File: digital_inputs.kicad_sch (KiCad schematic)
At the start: 11 parts, among them J2 Samtec Isorate Right Angle, J3 Samtec Isorate, U8 SN74LVC16244A-EP

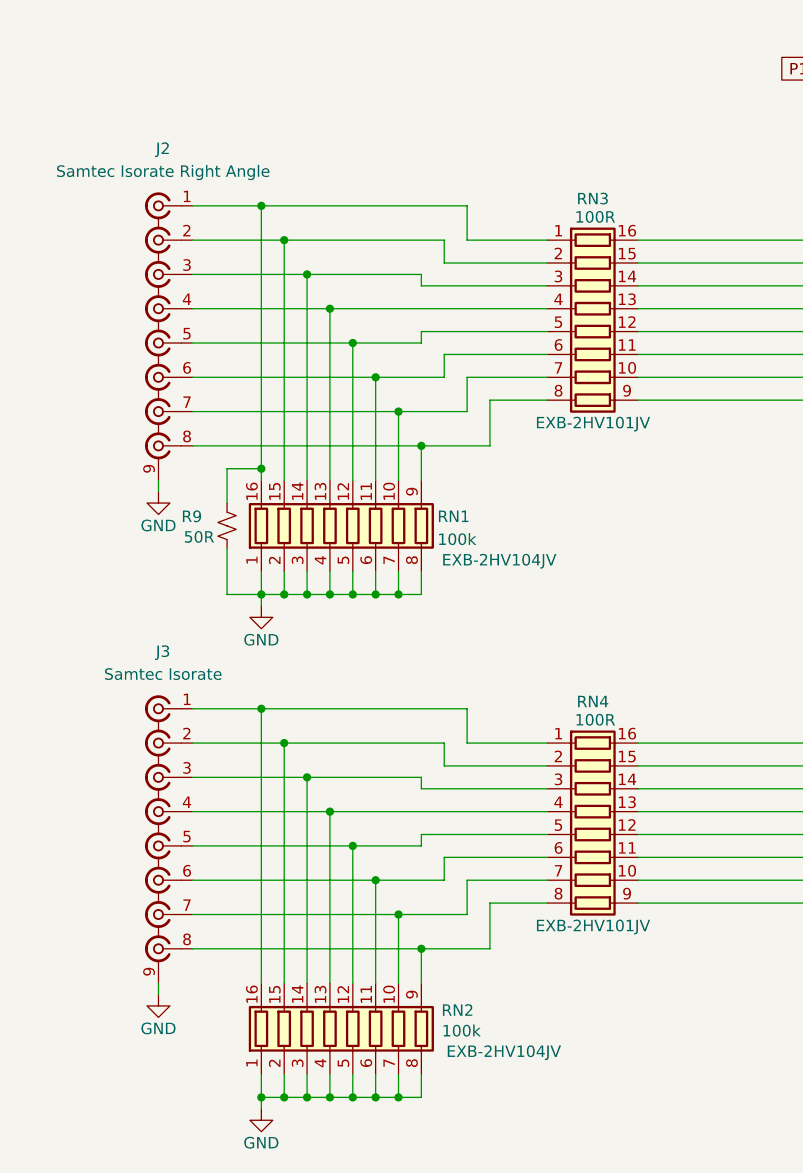
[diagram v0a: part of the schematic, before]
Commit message: Schematic updates
- Changed Connecters to MMCX
- Added Test points on clocks and data buses
- Added attenuation before the RF input level detection IC to better keep the recommended input within its linear range
- Added a low pass filter at the input of the RF input level detection IC
- grounded the thermal pad of the ADC
- added some additional decoupling caps in for the clock splitter chip (to be in line with what is on Zest)
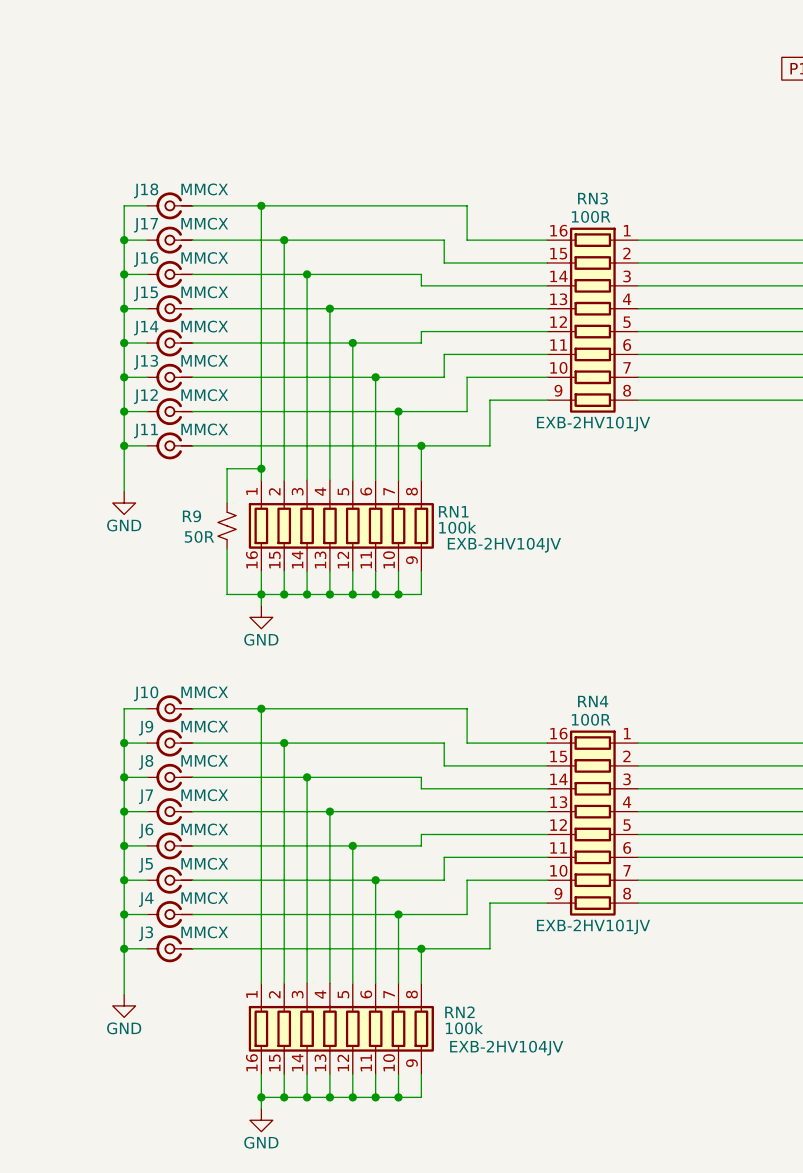
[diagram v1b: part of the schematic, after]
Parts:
- removed J2: Samtec Isorate Right Angle, rf-input-fmc:SAMTEC_IP5-08-01-L-S-RA1-L-TR, symbol rf-input-fmc:Isorate_8pin
- removed J3: Samtec Isorate, rf-input-fmc:SAMTEC_IP5-08-05.0-L-S-1-L-TR, symbol rf-input-fmc:Isorate_8pin
- added J10, J11, J12, J13, J14, J15, J16, J17, J18, J3, J4, J5, J6, J7, J8, J9: MMCX, Connector_Coaxial:MMCX_Molex_73415-1471_Vertical, symbol Connector:Conn_Coaxial_Small
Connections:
- net GND: now also RN1.10 (R7.2), RN1.11 (R6.2), RN1.12 (R5.2), RN1.13 (R4.2), RN1.14 (R3.2), RN1.15 (R2.2), RN1.16 (R1.2), RN1.9 (R8.2), RN2.10 (R7.2), RN2.11 (R6.2), RN2.12 (R5.2), RN2.13 (R4.2), RN2.14 (R3.2), RN2.15 (R2.2), RN2.16 (R1.2), RN2.9 (R8.2), J10.2 (Ext), J11.2 (Ext), J12.2 (Ext), J13.2 (Ext), J14.2 (Ext), J15.2 (Ext), J16.2 (Ext), J17.2 (Ext), J18.2 (Ext), J3.2 (Ext), J4.2 (Ext), J5.2 (Ext), J6.2 (Ext), J7.2 (Ext), J8.2 (Ext), J9.2 (Ext); no longer RN1.1 (R1.1), RN1.2 (R2.1), RN1.3 (R3.1), RN1.4 (R4.1), RN1.5 (R5.1), RN1.6 (R6.1), RN1.7 (R7.1), RN1.8 (R8.1), RN2.1 (R1.1), RN2.2 (R2.1), RN2.3 (R3.1), RN2.4 (R4.1), RN2.5 (R5.1), RN2.6 (R6.1), RN2.7 (R7.1), RN2.8 (R8.1)
- net at RN4.7 (R7.1): now also U8.27 (4A3); no longer RN2.10 (R7.2)
- net at RN4.6 (R6.1): now also U8.29 (4A2); no longer RN2.11 (R6.2)
- net at RN4.5 (R5.1): now also U8.30 (4A1); no longer RN2.12 (R5.2)
- net at RN4.4 (R4.1): now also U8.32 (3A4); no longer RN2.13 (R4.2)
- net at RN4.3 (R3.1): now also U8.33 (3A3); no longer RN2.14 (R3.2)
- net at RN4.2 (R2.1): now also U8.35 (3A2); no longer RN2.15 (R2.2)
- net at RN4.1 (R1.1): now also U8.36 (3A1); no longer RN2.16 (R1.2)
- net at RN4.8 (R8.1): now also U8.26 (4A4); no longer RN2.9 (R8.2)
- net at RN3.2 (R2.1): now also U8.46 (1A2); no longer RN1.15 (R2.2)
- net at RN3.3 (R3.1): now also U8.44 (1A3); no longer RN1.14 (R3.2)
- net at RN3.4 (R4.1): now also U8.43 (1A4); no longer RN1.13 (R4.2)
- net at RN3.5 (R5.1): now also U8.41 (2A1); no longer RN1.12 (R5.2)
- net at RN3.6 (R6.1): now also U8.40 (2A2); no longer RN1.11 (R6.2)
- net at RN3.7 (R7.1): now also U8.38 (2A3); no longer RN1.10 (R7.2)
- net at RN3.8 (R8.1): now also U8.37 (2A4); no longer RN1.9 (R8.2)
- net at RN4.9 (R8.2): now also RN2.8 (R8.1), J3.1 (In); no longer U8.26 (4A4)
- net at RN4.10 (R7.2): now also RN2.7 (R7.1), J4.1 (In); no longer U8.27 (4A3)
- net at RN4.11 (R6.2): now also RN2.6 (R6.1), J5.1 (In); no longer U8.29 (4A2)
- net at RN4.12 (R5.2): now also RN2.5 (R5.1), J6.1 (In); no longer U8.30 (4A1)
- net at RN4.13 (R4.2): now also RN2.4 (R4.1), J7.1 (In); no longer U8.32 (3A4)
- net at RN4.14 (R3.2): now also RN2.3 (R3.1), J8.1 (In); no longer U8.33 (3A3)
- net at RN4.15 (R2.2): now also RN2.2 (R2.1), J9.1 (In); no longer U8.35 (3A2)
- net at RN4.16 (R1.2): now also RN2.1 (R1.1), J10.1 (In); no longer U8.36 (3A1)
- net at RN3.9 (R8.2): now also RN1.8 (R8.1), J11.1 (In); no longer U8.37 (2A4)
- net at RN3.10 (R7.2): now also RN1.7 (R7.1), J12.1 (In); no longer U8.38 (2A3)
- net at RN3.11 (R6.2): now also RN1.6 (R6.1), J13.1 (In); no longer U8.40 (2A2)
- net at RN3.12 (R5.2): now also RN1.5 (R5.1), J14.1 (In); no longer U8.41 (2A1)
- net at RN3.13 (R4.2): now also RN1.4 (R4.1), J15.1 (In); no longer U8.43 (1A4)
- net at RN3.14 (R3.2): now also RN1.3 (R3.1), J16.1 (In); no longer U8.44 (1A3)
- net at RN3.15 (R2.2): now also RN1.2 (R2.1), J17.1 (In); no longer U8.46 (1A2)
- net at RN3.16 (R1.2): now also R9.1, RN1.1 (R1.1), J18.1 (In); no longer U8.47 (1A1)
- new net: RN3.1 (R1.1), U8.47 (1A1)
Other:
- moved on the sheet: RN3, RN4

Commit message: Updated BOM of all parts
Updated BOM of all parts
-added supplier & supplier part number to all parts
- fixed many issues with part including:R5-R8,C34,C35,C24, R10-R15

Changed filter C36&C37 to 15nF (keep COG & 0603, but changes filter cutoff to 3.8kHz|was 12kHz)
Changed bulk Caps to 22uF (was 47uF) to get a Cap with enough voltage headroom at 12V while 0805
Changed C31 to be a bulk 10uF cap
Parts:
- removed L7: 0603, Inductor_SMD:L_0603_1608Metric, symbol Device:L_Ferrite_Small
- C31: value 100nF -> 10uF; footprint Capacitor_SMD:C_0402_1005Metric -> Capacitor_SMD:C_0603_1608Metric; MPN GRM155R61A104KA01D -> GRM188R6YA106MA73D; Manufacturer Murata -> Murata Electronics; Supplier (none) -> Digikey; Supplier Part Number (none) -> 490-13248-1-ND
- C32: MPN GRM155R61A104KA01D -> GCM155R71H104KE02J; Manufacturer Murata -> Murata Electronics; Supplier (none) -> Digikey; Supplier Part Number (none) -> 490-14514-1-ND
- J10, J11, J12, J13, J14, J15, J16, J17, J18, J3, J4, J5, J6, J7, J8, J9: Supplier (none) -> Digikey; Supplier Part Number (none) -> SAM10617-ND
- R9: Supplier (none) -> Digikey; Supplier Part Number (none) -> 541-TNPW120650R0BEENCT-ND
- RN1, RN2: Supplier (none) -> Digikey; Supplier Part Number (none) -> Y1104CT-ND
- RN3, RN4: Supplier (none) -> Digikey; Supplier Part Number (none) -> Y1101CT-ND
- U8: Supplier (none) -> Digikey; Supplier Part Number (none) -> 296-36050-5-ND
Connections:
- net GND: now also C31.2; no longer C31.1
- net P1_VADJ: now also C31.1, C32.2, U8.18 (VCC), U8.31 (VCC), U8.42 (VCC), U8.7 (VCC)

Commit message: Finished Board Layout
Schematic Changes
- Removed some testpoints
- Fixed Lib issues
- moved around FMC pinout

Layout
- routed all traces
- routed RF traces using Controlled Impedance in mind
- ERC/DRC free
- All silkscreen is arranged

Still to do
- finish net-classes for controlled traces
- create arc traces for diff CLK lines
- small tweaks to improve RF performance
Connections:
- net D_Input11: now also U8.17 (3Y4); no longer U8.23 (4Y4)
- net D_Input12: now also U8.19 (4Y1); no longer U8.13 (3Y1)
- net D_Input15: now also U8.23 (4Y4); no longer U8.17 (3Y4)
- net D_Input8: now also U8.13 (3Y1); no longer U8.19 (4Y1)

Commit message: Tweaks to Layout/ fixed project errors
-Adjusted Testpoints by changing the value field to visible on the silkscreen layer.
- Fixed DRC and ERC issues

Known to do:
- run rounded traces
- determine neg/gnd pin of J20 (do we want to float but diff? SE?)
- determine/implement best practice grounding for mounting holes?
- Additional RF trace tweaking
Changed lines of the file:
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@@
 	)
 	(junction
-		(at 149.86 41.91)
-		(diameter 0)
-		(color 0 0 0 0)
-	)
-	(junction
 		(at 71.12 100.33)
 		(diameter 0)
@@
 					(unit 1)
 				)
-			)
-		)
-	)
-	(symbol
-		(lib_id "power:PWR_FLAG")
-		(at 149.86 41.91 270)
-		(mirror x)
-		(unit 1)
-		(exclude_from_sim no)
-		(in_bom yes)
-		(on_board yes)
-		(dnp no)
-		(fields_autoplaced yes)
-		(property "Reference" "#FLG04"
-			(at 151.765 41.91 0)
-			(effects
-				(font
-					(size 1.27 1.27)
-				)
-				(hide yes)
-			)
-		)
-		(property "Value" "PWR_FLAG"
-			(at 153.67 41.9099 90)
-			(effects
-				(font
-					(size 1.27 1.27)
-				)
-				(justify left)
-			)
-		)
-		(property "Footprint" ""
-			(at 149.86 41.91 0)
-			(effects
-				(font
-					(size 1.27 1.27)
-				)
-				(hide yes)
-			)
-		)
-		(property "Datasheet" "~"
-			(at 149.86 41.91 0)
-			(effects
-				(font
-					(size 1.27 1.27)
-				)
-				(hide yes)
-			)
-		)
-		(property "Description" "Special symbol for telling ERC where power comes from"
-			(at 149.86 41.91 0)
-			(effects
-				(font
-					(size 1.27 1.27)
-				)
-				(hide yes)
-			)
-		)
-		(pin "1"
-		)
-		(instances
-			(project "rf-input-fmc"
-				(path "/1719e569-47c8-4fa0-8523-9c9686ef0dba/4cafb3fc-40db-4b97-9099-60c0c4fd2349"
-					(reference "#FLG04")
-					(unit 1)
-				)

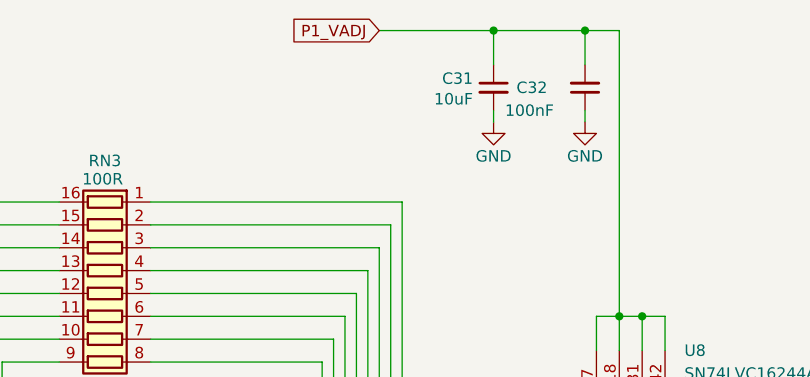
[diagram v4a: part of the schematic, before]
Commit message: Final Draft for prototype run
- Updated CLK mapping to FMC
	 - Now Output 12 goes to M2C CLK instead of a GBT CLK
	 - Outputs 0, 4, 8 have moved
	 - all CLK now have polarity swapped at the FMC pin
		 - CLK signals maintain normal polarity through the CLK distribution chip but are now ALL swapped between the CLK Distribution IC output and the FMC pins
	- Added a monitor output on Output13 (J20)
- Moved decoupling caps to bottom of LCB in many places
- Standardized the area to the right of the FMC to use as a future template
- Moved board specific test points and function to the left
- Added an additional bypass cap on U8
- Tied the front two mounting hole (H3 &H4) to GND
- changed H2 to be a slotted hole
	- This allows for mounting in the FMC slot on Marble where to the mounting hole is shifted by ~4mil
- Add Serial Number area and Board title
- Cleaned up all silkscreen and Fab layers
- Changed J1 & J2 to SMA
	- Added 3d model (from manufacture) to footprint
-  Moved many of the major layout blocks to allow for other changes in this commit
- Added power planes for many major and minor distributed power rails
- pulled back power planes from input connectors
- Fixed all ERC & DRC errors/warnings
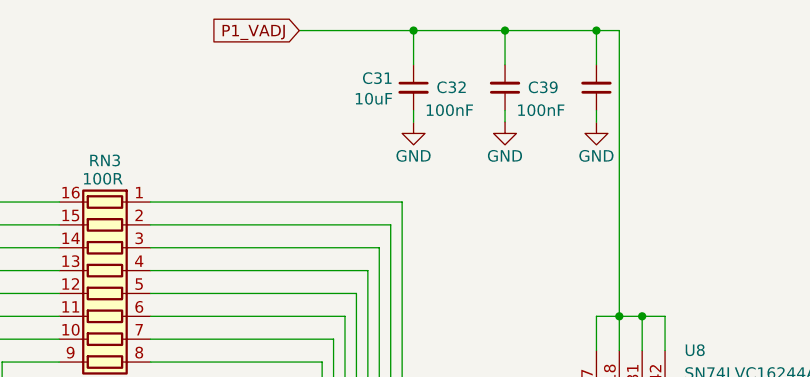
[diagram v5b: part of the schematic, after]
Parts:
- added C39: 100nF, Capacitor_SMD:C_0402_1005Metric, symbol Device:C_Small
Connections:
- net GND: now also C39.1
- net P1_VADJ: now also C39.2
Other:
- moved on the sheet: C31, C32

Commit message: Prototype Production Ready
- Removed Supplier and Supplier Part Numbers for project
- Changed Kibot to not out Supplier and Supplier Part Numbers for project
- Changed a few ignored ERC/DRC testing to warnings, and found no additional issues
- project is ready for production
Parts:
- C31: Supplier Digikey -> (none); Supplier Part Number 490-13248-1-ND -> (none)
- C32, C39: Supplier Digikey -> (none); Supplier Part Number 490-14514-1-ND -> (none)
- J10, J11, J12, J13, J14, J15, J16, J17, J18, J3, J4, J5, J6, J7, J8, J9: Supplier Digikey -> (none); Supplier Part Number SAM10617-ND -> (none)
- R9: Supplier Digikey -> (none); Supplier Part Number 541-TNPW120650R0BEENCT-ND -> (none)
- RN1, RN2: Supplier Digikey -> (none); Supplier Part Number Y1104CT-ND -> (none)
- RN3, RN4: Supplier Digikey -> (none); Supplier Part Number Y1101CT-ND -> (none)
- U8: Supplier Digikey -> (none); Supplier Part Number 296-36050-5-ND -> (none)
